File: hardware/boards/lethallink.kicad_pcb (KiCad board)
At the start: 6 copper layers, 86 x 111.1 mm, 111 parts, among them J1 PCIe-x4, J2 USB3_Micro_B_Amphenol, Q1 Q_NMOS_GSD, Q2 Q_NMOS_GSD, Q3 Q_NMOS_GSD, Q4 Q_NMOS_GSD, Q5 SI7232DN-T1-GE3, SW1 SW_DIP_x03, U1 ECP5UM5G-381caBGA, U2 ADP5050ACPZ-R7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

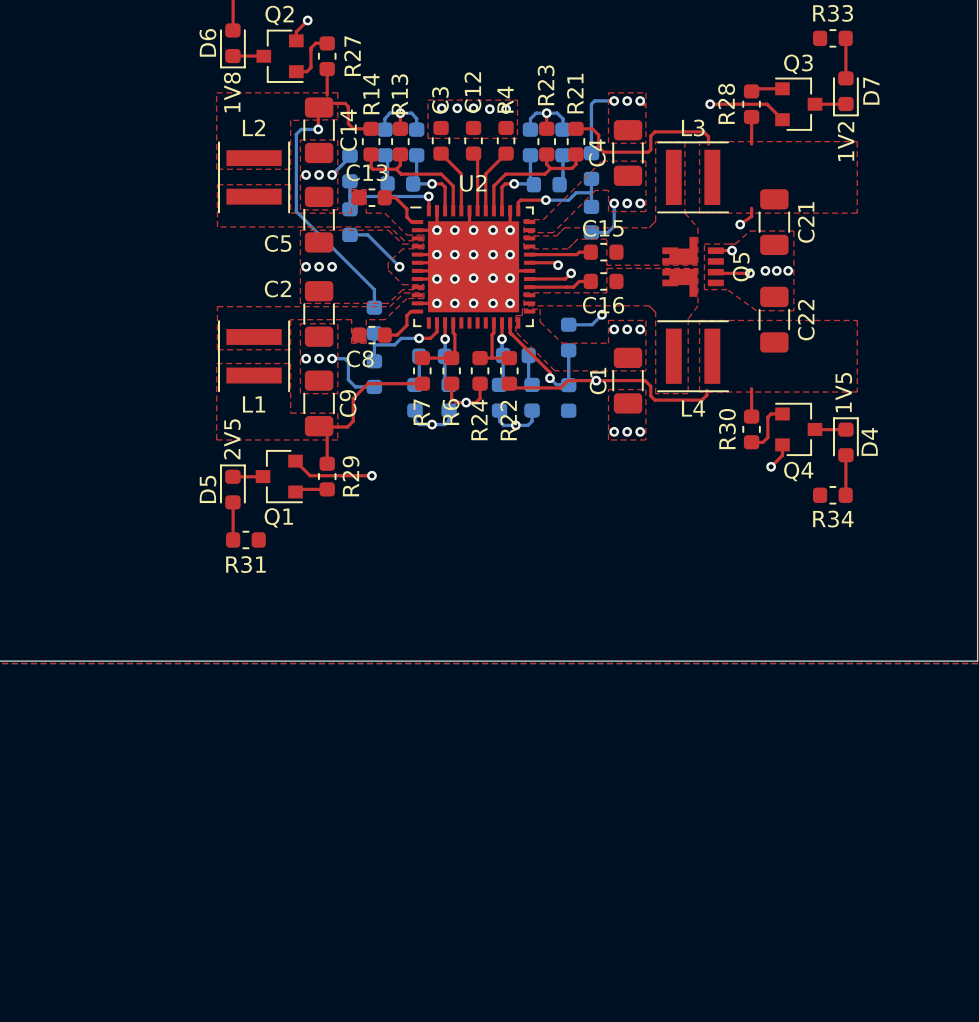
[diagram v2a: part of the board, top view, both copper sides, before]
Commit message: Added test points for the various voltage rails
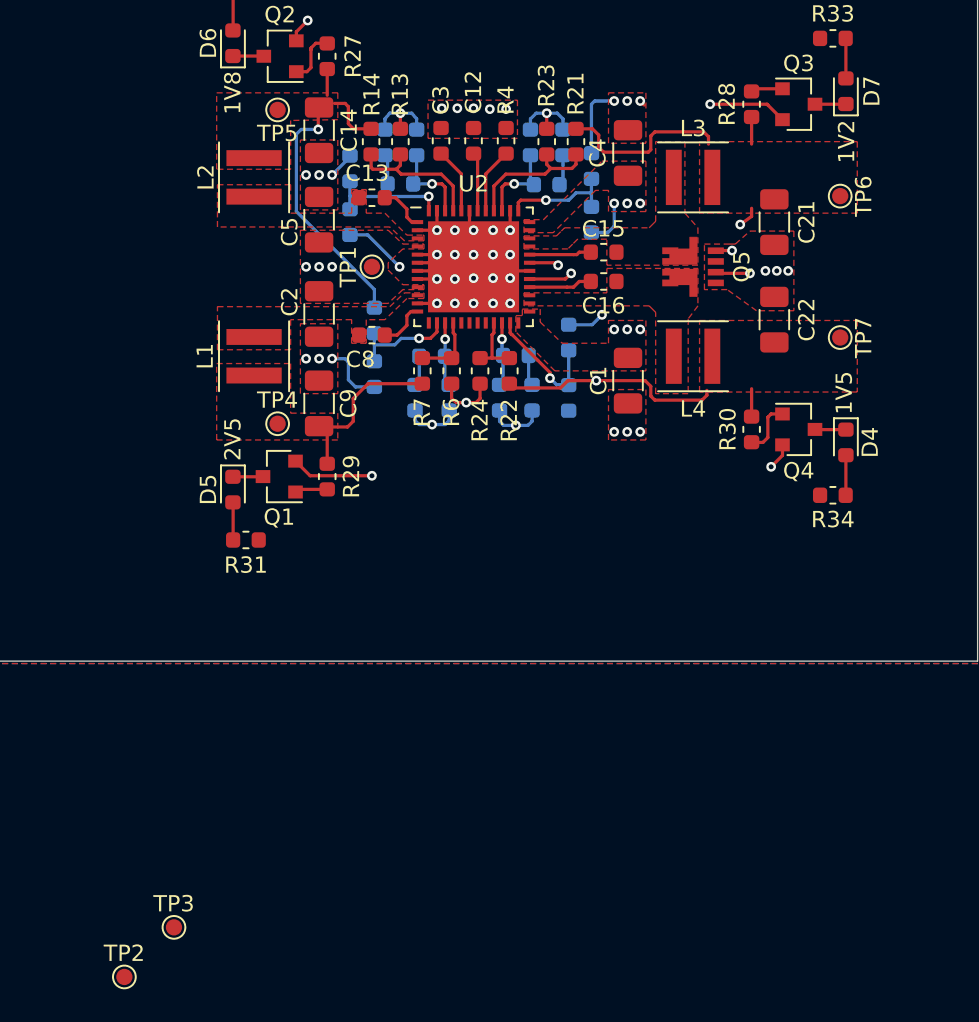
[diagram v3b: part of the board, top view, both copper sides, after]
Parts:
- added TP1: 12v0, TestPoint:TestPoint_Pad_D1.0mm, F.Cu at (147.6, 89.8)
- added TP2: 3v3, TestPoint:TestPoint_Pad_D1.0mm, F.Cu at (132.4, 133.5)
- added TP3: 3v3 Aux, TestPoint:TestPoint_Pad_D1.0mm, F.Cu at (135.4, 130.5)
- added TP4: 2v5, TestPoint:TestPoint_Pad_D1.0mm, F.Cu at (141.8, 99.5)
- added TP5: 1v8, TestPoint:TestPoint_Pad_D1.0mm, F.Cu at (141.8, 80.2)
- added TP6: 1v2, TestPoint:TestPoint_Pad_D1.0mm, F.Cu at (176.4, 85.5)
- added TP7: 1v5, TestPoint:TestPoint_Pad_D1.0mm, F.Cu at (176.4, 94.2)
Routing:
- added copper zone on In4.Cu, net Net-(C39-Pad2)
- removed copper zone on In4.Cu, net /PCIe Interface/TX0_P
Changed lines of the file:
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@@
     (tracks 393)
     (zones 0)
-    (modules 111)
+    (modules 118)
     (nets 519)
   )
@@
   )
   (setup
-    (last_trace_width 0.2)
+    (last_trace_width 0.1524)
+    (user_trace_width 0.1524)
     (user_trace_width 0.2)
+    (user_trace_width 0.3)
+    (user_trace_width 0.4)
+    (user_trace_width 0.6)
+    (user_trace_width 0.8)
+    (user_trace_width 1)
     (trace_clearance 0.2)
     (zone_clearance 0.1)
@@
     (add_net "Net-(U5-Pad8)")
   )
+  (module TestPoint:TestPoint_Pad_D1.0mm (layer F.Cu)
+    (at 176.4 94.2 270)
+    (descr "SMD pad as test Point, diameter 1.0mm")
+    (tags "test point SMD pad")
+    (attr virtual)
+    (fp_text reference TP7 (at 0 -1.448 90) (layer F.SilkS)
+      (effects (font (size 1 1) (thickness 0.15)))
+    )
+    (fp_text value 1v5 (at 0 1.55 90) (layer F.Fab)
+      (effects (font (size 1 1) (thickness 0.15)))
+    )
+    (fp_text user %R (at 0 -1.45 90) (layer F.Fab)
+      (effects (font (size 1 1) (thickness 0.15)))
+    )
+    (fp_circle (center 0 0) (end 1 0) (layer F.CrtYd) (width 0.05))
+    (fp_circle (center 0 0) (end 0 0.7) (layer F.SilkS) (width 0.12))
+    (pad 1 smd circle (at 0 0 270) (size 1 1) (layers F.Cu F.Mask)
+      (net 30 +1V5))
+  )
+  (module TestPoint:TestPoint_Pad_D1.0mm (layer F.Cu)
+    (at 176.4 85.5 270)
+    (descr "SMD pad as test Point, diameter 1.0mm")
+    (tags "test point SMD pad")
+    (attr virtual)
+    (fp_text reference TP6 (at 0 -1.448 90) (layer F.SilkS)
+      (effects (font (size 1 1) (thickness 0.15)))
+    )
+    (fp_text value 1v2 (at 0 1.55 90) (layer F.Fab)
+      (effects (font (size 1 1) (thickness 0.15)))
+    )
+    (fp_text user %R (at 0 -1.45 90) (layer F.Fab)
+      (effects (font (size 1 1) (thickness 0.15)))
+    )
+    (fp_circle (center 0 0) (end 1 0) (layer F.CrtYd) (width 0.05))
+    (fp_circle (center 0 0) (end 0 0.7) (layer F.SilkS) (width 0.12))
+    (pad 1 smd circle (at 0 0 270) (size 1 1) (layers F.Cu F.Mask)
+      (net 29 +1V2))
+  )
+  (module TestPoint:TestPoint_Pad_D1.0mm (layer F.Cu)
+    (at 141.8 80.2 180)
+    (descr "SMD pad as test Point, diameter 1.0mm")
+    (tags "test point SMD pad")
+    (attr virtual)
+    (fp_text reference TP5 (at 0 -1.448) (layer F.SilkS)
+      (effects (font (size 1 1) (thickness 0.15)))
+    )
+    (fp_text value 1v8 (at 0 1.55) (layer F.Fab)
+      (effects (font (size 1 1) (thickness 0.15)))
+    )
+    (fp_text user %R (at 0 -1.45) (layer F.Fab)
+      (effects (font (size 1 1) (thickness 0.15)))
+    )
+    (fp_circle (center 0 0) (end 1 0) (layer F.CrtYd) (width 0.05))
+    (fp_circle (center 0 0) (end 0 0.7) (layer F.SilkS) (width 0.12))
+    (pad 1 smd circle (at 0 0 180) (size 1 1) (layers F.Cu F.Mask)
+      (net 20 +1V8))
+  )
+  (module TestPoint:TestPoint_Pad_D1.0mm (layer F.Cu)
+    (at 141.8 99.5)
+    (descr "SMD pad as test Point, diameter 1.0mm")
+    (tags "test point SMD pad")
+    (attr virtual)
+    (fp_text reference TP4 (at 0 -1.448) (layer F.SilkS)
+      (effects (font (size 1 1) (thickness 0.15)))
+    )
+    (fp_text value 2v5 (at 0 1.55) (layer F.Fab)
+      (effects (font (size 1 1) (thickness 0.15)))
+    )
+    (fp_text user %R (at 0 -1.45) (layer F.Fab)
+      (effects (font (size 1 1) (thickness 0.15)))
+    )
+    (fp_circle (center 0 0) (end 1 0) (layer F.CrtYd) (width 0.05))
+    (fp_circle (center 0 0) (end 0 0.7) (layer F.SilkS) (width 0.12))
+    (pad 1 smd circle (at 0 0) (size 1 1) (layers F.Cu F.Mask)
+      (net 14 +2V5))
+  )
+  (module TestPoint:TestPoint_Pad_D1.0mm (layer F.Cu)
+    (at 135.425001 130.475001)
+    (descr "SMD pad as test Point, diameter 1.0mm")
+    (tags "test point SMD pad")
+    (attr virtual)
+    (fp_text reference TP3 (at 0 -1.448) (layer F.SilkS)
+      (effects (font (size 1 1) (thickness 0.15)))
+    )
+    (fp_text value "3v3 Aux" (at 0 1.55) (layer F.Fab)
+      (effects (font (size 1 1) (thickness 0.15)))
+    )
+    (fp_text user %R (at 0 -1.45) (layer F.Fab)
+      (effects (font (size 1 1) (thickness 0.15)))
+    )
+    (fp_circle (center 0 0) (end 1 0) (layer F.CrtYd) (width 0.05))
+    (fp_circle (center 0 0) (end 0 0.7) (layer F.SilkS) (width 0.12))
+    (pad 1 smd circle (at 0 0) (size 1 1) (layers F.Cu F.Mask)
+      (net 6 +3.3VA))
+  )
+  (module TestPoint:TestPoint_Pad_D1.0mm (layer F.Cu)
+    (at 132.375001 133.525001)
+    (descr "SMD pad as test Point, diameter 1.0mm")
+    (tags "test point SMD pad")
+    (attr virtual)
+    (fp_text reference TP2 (at 0 -1.448) (layer F.SilkS)
+      (effects (font (size 1 1) (thickness 0.15)))
+    )
+    (fp_text value 3v3 (at 0 1.55) (layer F.Fab)
+      (effects (font (size 1 1) (thickness 0.15)))
+    )
+    (fp_text user %R (at 0 -1.45) (layer F.Fab)
+      (effects (font (size 1 1) (thickness 0.15)))
+    )
+    (fp_circle (center 0 0) (end 1 0) (layer F.CrtYd) (width 0.05))
+    (fp_circle (center 0 0) (end 0 0.7) (layer F.SilkS) (width 0.12))
+    (pad 1 smd circle (at 0 0) (size 1 1) (layers F.Cu F.Mask)
+      (net 7 +3V3))
+  )
+  (module TestPoint:TestPoint_Pad_D1.0mm (layer F.Cu)
+    (at 147.6 89.85 90)
+    (descr "SMD pad as test Point, diameter 1.0mm")
+    (tags "test point SMD pad")
+    (attr virtual)
+    (fp_text reference TP1 (at 0 -1.448 90) (layer F.SilkS)
+      (effects (font (size 1 1) (thickness 0.15)))
+    )
+    (fp_text value 12v0 (at 0 1.55 90) (layer F.Fab)
+      (effects (font (size 1 1) (thickness 0.15)))
+    )
+    (fp_text user %R (at 0 -1.45 90) (layer F.Fab)
+      (effects (font (size 1 1) (thickness 0.15)))
+    )
+    (fp_circle (center 0 0) (end 1 0) (layer F.CrtYd) (width 0.05))
+    (fp_circle (center 0 0) (end 0 0.7) (layer F.SilkS) (width 0.12))
+    (pad 1 smd circle (at 0 0 90) (size 1 1) (layers F.Cu F.Mask)
+      (net 8 +12V))
+  )
   (module Resistor_SMD:R_0603_1608Metric (layer F.Cu)
     (at 64.15 110.5)
@@
     (tags "L Coilcraft XxL4030")
     (attr smd)
-    (fp_text reference L2 (at -3 0) (layer F.SilkS)
+    (fp_text reference L2 (at 0 2.95 90) (layer F.SilkS)
       (effects (font (size 1 1) (thickness 0.15)))
     )
@@
     (tags "L Coilcraft XxL4040")
     (attr smd)
-    (fp_text reference L1 (at -3 0) (layer F.SilkS)
+    (fp_text reference L1 (at 0 -3 90) (layer F.SilkS)
       (effects (font (size 1 1) (thickness 0.15)))
     )
@@
     (tags capacitor)
     (attr smd)
-    (fp_text reference C5 (at 1.5 2.5) (layer F.SilkS)
+    (fp_text reference C5 (at 0.75 1.8 90) (layer F.SilkS)
       (effects (font (size 1 1) (thickness 0.15)))
     )
@@
     (tags capacitor)
     (attr smd)
-    (fp_text reference C2 (at 1.5 -2.5 180) (layer F.SilkS)
+    (fp_text reference C2 (at 0.75 -1.8 270) (layer F.SilkS)
       (effects (font (size 1 1) (thickness 0.15)))
     )
@@
     )
   )
-  (zone (net 31) (net_name "/PCIe Interface/TX0_P") (layer In4.Cu) (hatch edge 0.508)
+  (zone (net 31) (net_name "Net-(C39-Pad2)") (layer In4.Cu) (hatch edge 0.508)
     (priority 2)
     (connect_pads yes (clearance 0.1))

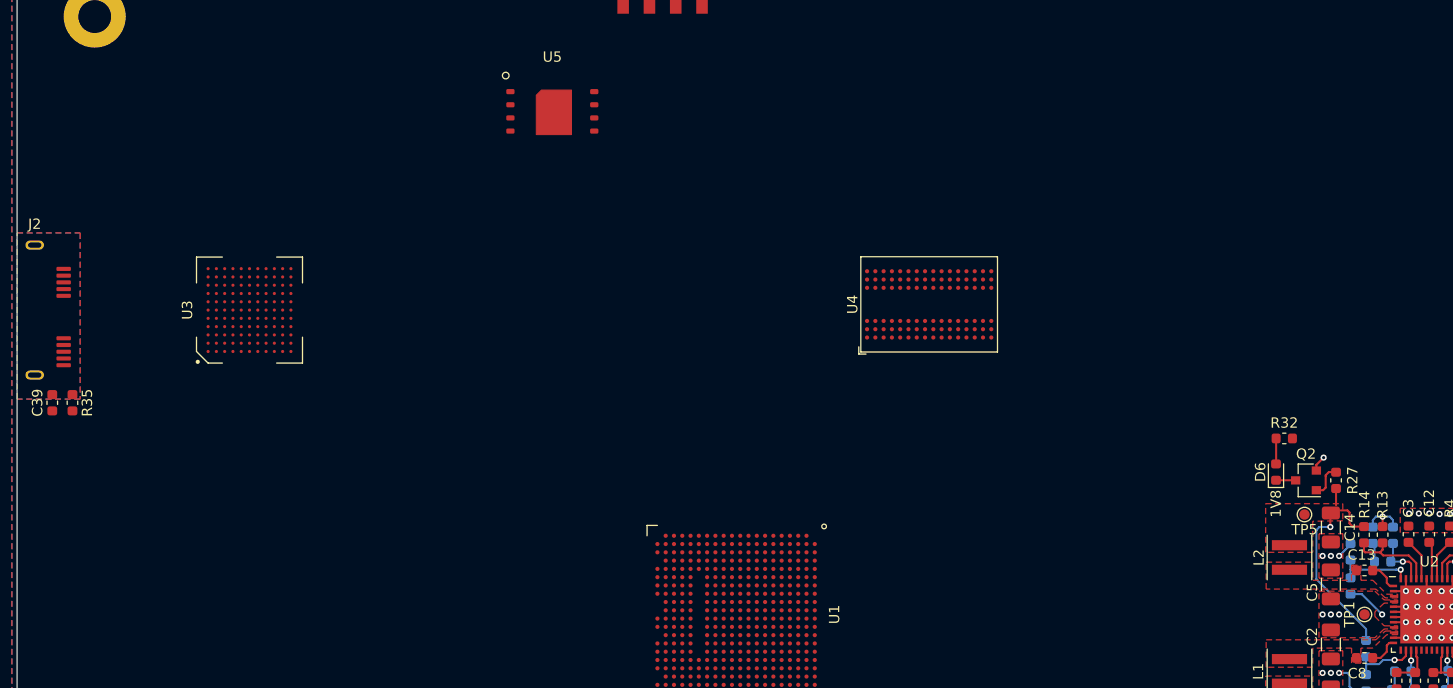
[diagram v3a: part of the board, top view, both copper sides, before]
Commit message: In an AHDH fuled stupor I made a bunch of changes, only the last of which I recall, which would be adding fiducials
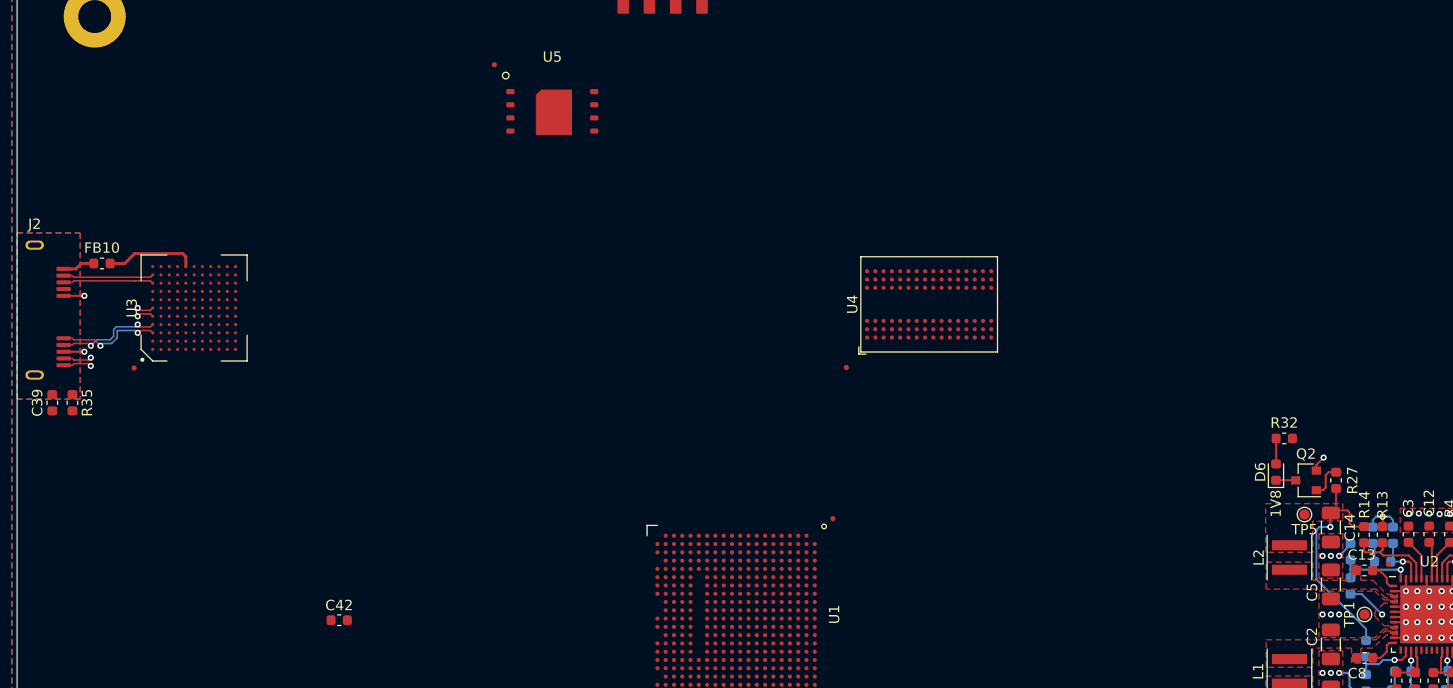
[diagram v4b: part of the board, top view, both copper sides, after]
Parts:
- added C42: 0.1uF, Capacitor_SMD:C_0603_1608Metric, F.Cu at (48.6, 90.4)
- added FB10: 220 @ 100Mhz, Resistor_SMD:R_0603_1608Metric, F.Cu at (25.6, 56.0)
- added FID1: Fiducial, Fiducial:Fiducial_0.5mm_Mask1mm, F.Cu at (28.8, 66.0)
- added FID2: Fiducial, Fiducial:Fiducial_0.5mm_Mask1mm, F.Cu at (149.9, 85.0)
- added FID3: Fiducial, Fiducial:Fiducial_0.5mm_Mask1mm, F.Cu at (96.2, 80.6)
- added FID4: Fiducial, Fiducial:Fiducial_0.5mm_Mask1mm, F.Cu at (63.5, 36.8)
- added FID5: Fiducial, Fiducial:Fiducial_0.5mm_Mask1mm, F.Cu at (97.5, 66.0)
- moved U3 5.35 mm to (34.5, 60.2)
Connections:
- net Net-(J2-Pad2) renamed /USB3 Interface/D-
- net Net-(J2-Pad3) renamed /USB3 Interface/D+
- J2 pad 1: Net-(J2-Pad1) -> /USB3 Interface/VBUS
- J2 pad 10: Net-(J2-Pad10) -> /USB3 Interface/SSTX+
- J2 pad 6: Net-(J2-Pad6) -> /USB3 Interface/SSRX-
- J2 pad 7: Net-(J2-Pad7) -> /USB3 Interface/SSRX+
- J2 pad 9: Net-(J2-Pad9) -> /USB3 Interface/SSTX-
- U3 pad A3: Net-(J2-Pad9) -> /USB3 Interface/SSRX-
- U3 pad A4: Net-(J2-Pad10) -> /USB3 Interface/SSRX+
- U3 pad A5: Net-(J2-Pad7) -> /USB3 Interface/SSTX+
- U3 pad A6: Net-(J2-Pad6) -> /USB3 Interface/SSTX-
- U3 pad E11: Net-(U3-PadE11) -> /IC Power/VBUS
- U5 pad 4: Net-(U5-Pad4) -> GND
- U5 pad 8: Net-(U5-Pad8) -> +3V3
- U5 pad 9: Net-(U5-Pad4) -> GND
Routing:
- net /USB3 Interface/SSTX-: track 0.00 -> 13.1 mm, vias 0 -> 2
- net /USB3 Interface/SSTX+: track 0.00 -> 13.1 mm, vias 0 -> 2
- net /USB3 Interface/SSRX-: track 0.00 -> 10.2 mm, vias 0 -> 2
- net /USB3 Interface/SSRX+: track 0.00 -> 10.2 mm, vias 0 -> 2
- net /USB3 Interface/D+: track 0.00 -> 8.90 mm
- net /USB3 Interface/D-: track 0.00 -> 8.90 mm
- net /IC Power/VBUS: track 0.00 -> 8.78 mm
- net GND: track 55.5 -> 59.5 mm, vias 49 -> 51
- net /USB3 Interface/VBUS: track 0.00 -> 3.07 mm
